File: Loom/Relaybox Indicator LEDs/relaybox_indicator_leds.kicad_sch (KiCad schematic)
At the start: 37 parts, among them J1 Conn_01x08_Pin, J2 Conn_01x08_Pin, SW1 SW_DPDT_x2, SW2 SW_DPDT_x2, SW3 SW_DPDT_x2, SW4 SW_DPDT_x2, SW5 SW_DPDT_x2, SW6 SW_DPDT_x2, SW7 SW_DPDT_x2

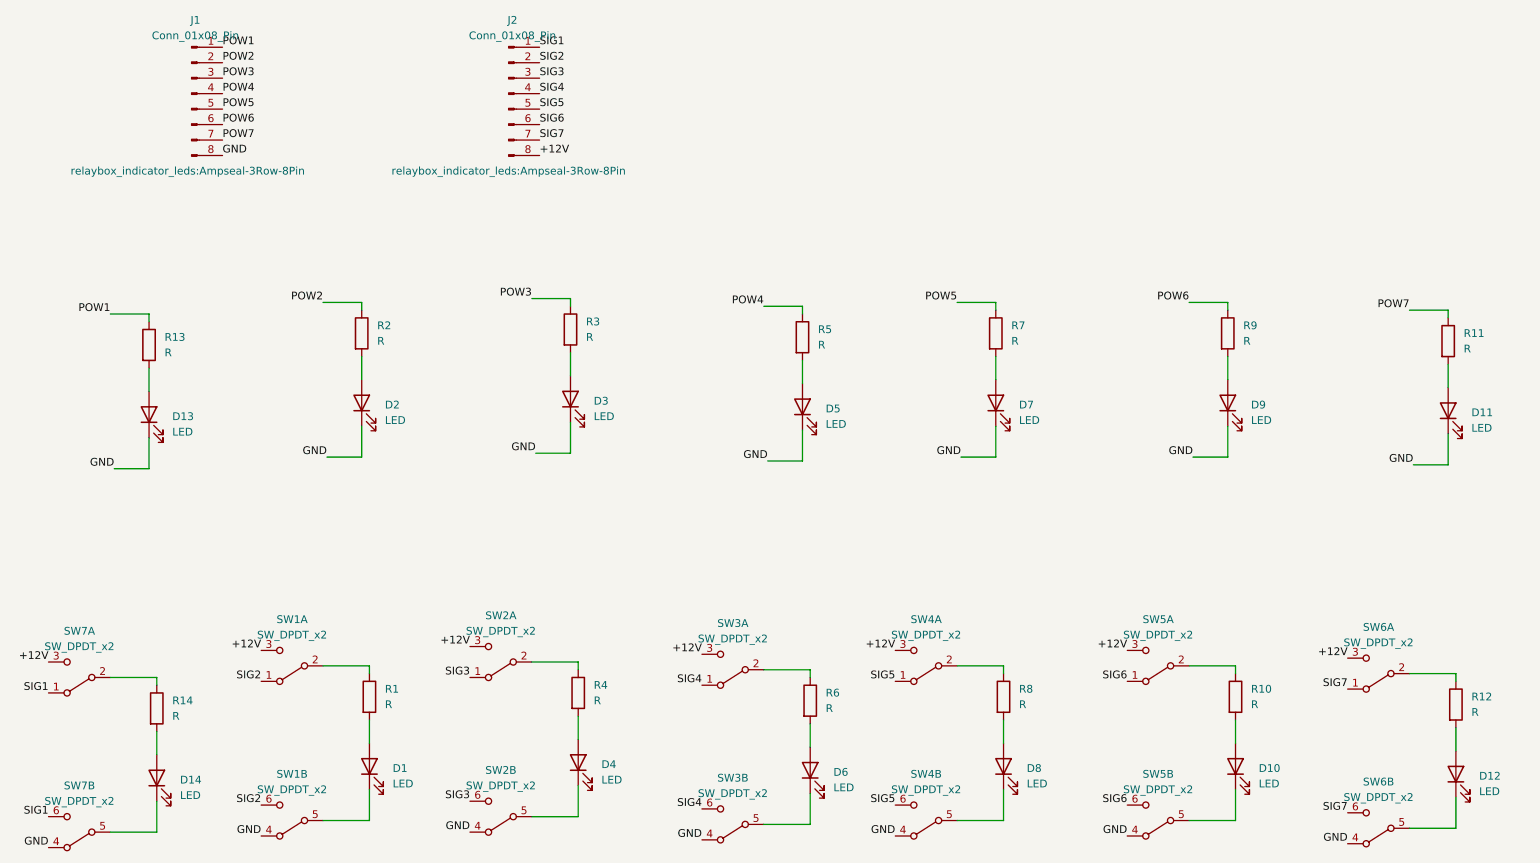
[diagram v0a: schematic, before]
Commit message: Added footprints and fixed component numbering
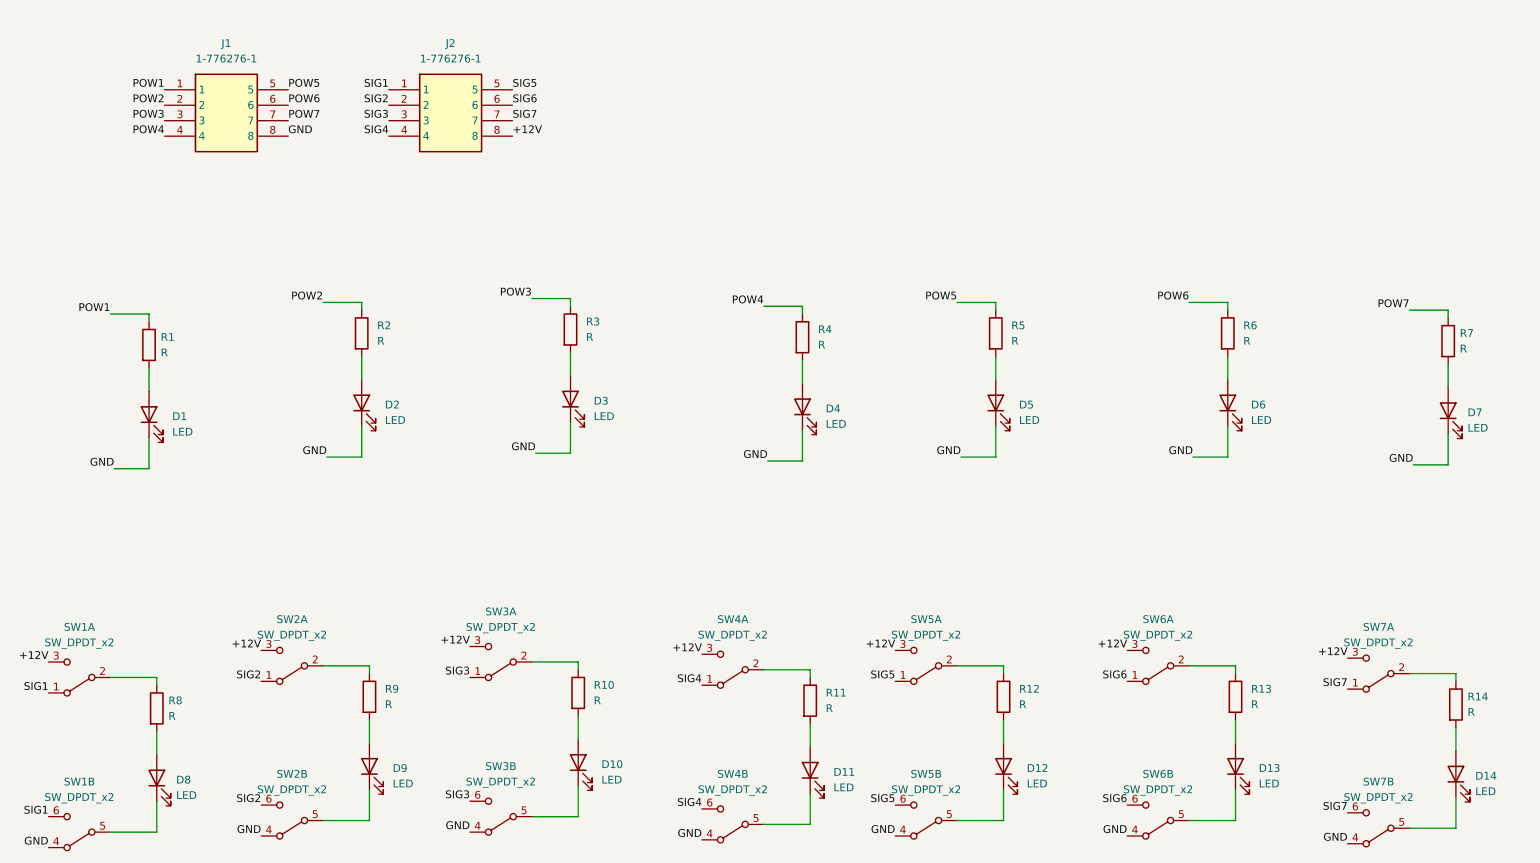
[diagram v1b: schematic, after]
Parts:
- removed J1, J2: Conn_01x08_Pin, relaybox_indicator_leds:Ampseal-3Row-8Pin, symbol Connector:Conn_01x08_Pin
- added J1, J2: 1-776276-1, relaybox_indicator_leds:17762761, symbol 1-776276-1:1-776276-1
- D1: renamed from D13; footprint (none) -> LED_THT:LED_D5.0mm
- D10: renamed from D4; footprint (none) -> LED_THT:LED_D5.0mm
- D11: renamed from D6; footprint (none) -> LED_THT:LED_D5.0mm
- D12: renamed from D8; footprint (none) -> LED_THT:LED_D5.0mm
- D13: renamed from D10; footprint (none) -> LED_THT:LED_D5.0mm
- D14: renamed from D12; footprint (none) -> LED_THT:LED_D5.0mm
- D2, D3: footprint (none) -> LED_THT:LED_D5.0mm
- D4: renamed from D5; footprint (none) -> LED_THT:LED_D5.0mm
- D5: renamed from D7; footprint (none) -> LED_THT:LED_D5.0mm
- D6: renamed from D9; footprint (none) -> LED_THT:LED_D5.0mm
- D7: renamed from D11; footprint (none) -> LED_THT:LED_D5.0mm
- D8: renamed from D14; footprint (none) -> LED_THT:LED_D5.0mm
- D9: renamed from D1; footprint (none) -> LED_THT:LED_D5.0mm
- R1: renamed from R13; footprint (none) -> Resistor_THT:R_Axial_DIN0207_L6.3mm_D2.5mm_P10.16mm_Horizontal
- R10: renamed from R4; footprint (none) -> Resistor_THT:R_Axial_DIN0207_L6.3mm_D2.5mm_P10.16mm_Horizontal
- R11: renamed from R6; footprint (none) -> Resistor_THT:R_Axial_DIN0207_L6.3mm_D2.5mm_P10.16mm_Horizontal
- R12: renamed from R8; footprint (none) -> Resistor_THT:R_Axial_DIN0207_L6.3mm_D2.5mm_P10.16mm_Horizontal
- R13: renamed from R10; footprint (none) -> Resistor_THT:R_Axial_DIN0207_L6.3mm_D2.5mm_P10.16mm_Horizontal
- R14: renamed from R12; footprint (none) -> Resistor_THT:R_Axial_DIN0207_L6.3mm_D2.5mm_P10.16mm_Horizontal
- R2, R3: footprint (none) -> Resistor_THT:R_Axial_DIN0207_L6.3mm_D2.5mm_P10.16mm_Horizontal
- R4: renamed from R5; footprint (none) -> Resistor_THT:R_Axial_DIN0207_L6.3mm_D2.5mm_P10.16mm_Horizontal
- R5: renamed from R7; footprint (none) -> Resistor_THT:R_Axial_DIN0207_L6.3mm_D2.5mm_P10.16mm_Horizontal
- R6: renamed from R9; footprint (none) -> Resistor_THT:R_Axial_DIN0207_L6.3mm_D2.5mm_P10.16mm_Horizontal
- R7: renamed from R11; footprint (none) -> Resistor_THT:R_Axial_DIN0207_L6.3mm_D2.5mm_P10.16mm_Horizontal
- R8: renamed from R14; footprint (none) -> Resistor_THT:R_Axial_DIN0207_L6.3mm_D2.5mm_P10.16mm_Horizontal
- R9: renamed from R1; footprint (none) -> Resistor_THT:R_Axial_DIN0207_L6.3mm_D2.5mm_P10.16mm_Horizontal
- SW1: renamed from SW7; footprint (none) -> relaybox_indicator_leds:MP004696
- SW2: renamed from SW1; footprint (none) -> relaybox_indicator_leds:MP004696
- SW3: renamed from SW2; footprint (none) -> relaybox_indicator_leds:MP004696
- SW4: renamed from SW3; footprint (none) -> relaybox_indicator_leds:MP004696
- SW5: renamed from SW4; footprint (none) -> relaybox_indicator_leds:MP004696
- SW6: renamed from SW5; footprint (none) -> relaybox_indicator_leds:MP004696
- SW7: renamed from SW6; footprint (none) -> relaybox_indicator_leds:MP004696
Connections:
- net +12V: now also J2.8
- net GND: now also J1.8
- net POW1: now also J1.1
- net POW2: now also J1.2
- net POW3: now also J1.3
- net POW4: now also J1.4
- net POW5: now also J1.5
- net POW6: now also J1.6
- net POW7: now also J1.7
- net SIG1: now also J2.1
- net SIG2: now also J2.2
- net SIG3: now also J2.3
- net SIG4: now also J2.4
- net SIG5: now also J2.5
- net SIG6: now also J2.6
- net SIG7: now also J2.7

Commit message: PCB design
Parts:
- added TP1, TP10, TP11, TP12, TP13, TP14, TP15, TP2, TP3, TP4, TP5, TP6, TP7, TP8, TP9: TestPoint, TestPoint:TestPoint_THTPad_D3.0mm_Drill1.5mm, symbol Connector:TestPoint
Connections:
- net GND: now also TP15.1
- net POW1: now also TP1.1
- net POW2: now also TP2.1
- net POW3: now also TP3.1
- net POW4: now also TP4.1
- net POW5: now also TP5.1
- net POW6: now also TP6.1
- net POW7: now also TP7.1
- net SIG1: now also TP8.1
- net SIG2: now also TP9.1
- net SIG3: now also TP10.1
- net SIG4: now also TP11.1
- net SIG5: now also TP12.1
- net SIG6: now also TP13.1
- net SIG7: now also TP14.1
